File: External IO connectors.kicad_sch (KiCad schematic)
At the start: 2 parts

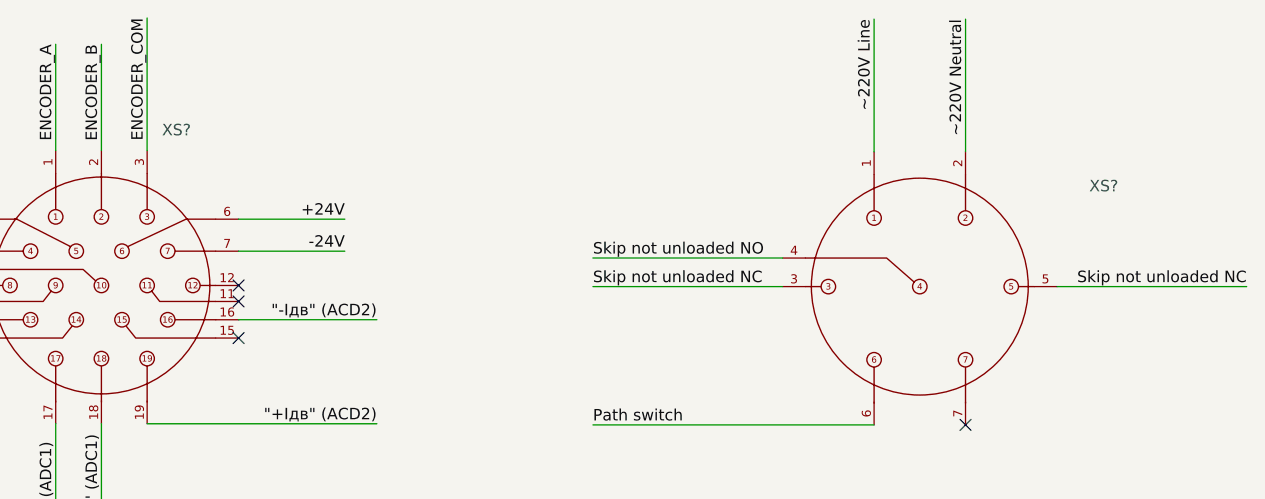
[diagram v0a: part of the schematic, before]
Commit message: Skip unload COM signal of external connector corrected
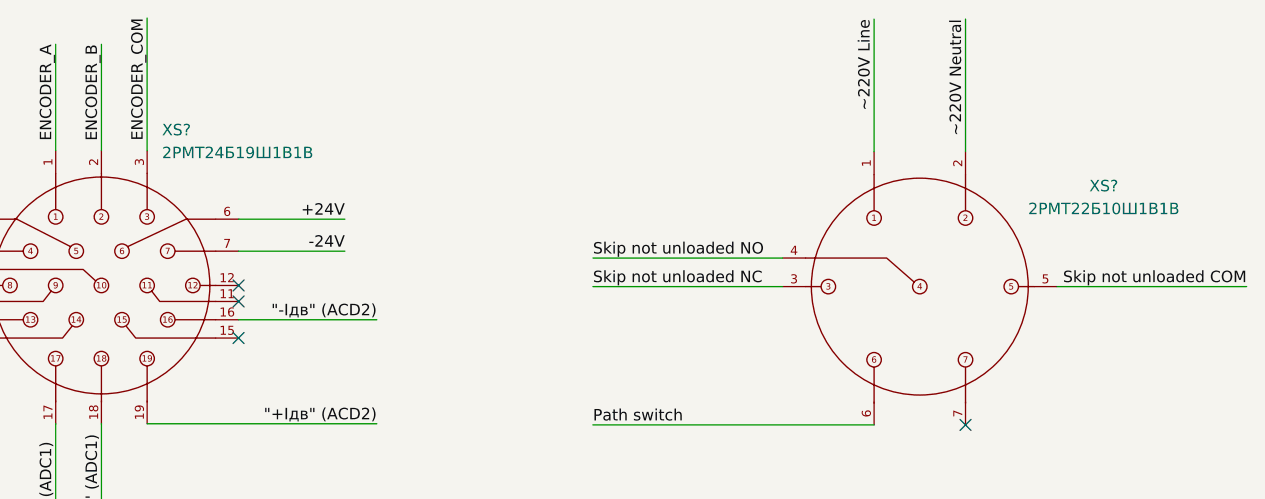
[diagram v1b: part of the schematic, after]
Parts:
- XS?: value (none) -> 2РМТ22Б10Ш1В1В
- XS?: value (none) -> 2РМТ24Б19Ш1В1В
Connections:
- net Skip not unloaded NC: no longer XS?.5
- new net Skip not unloaded COM: XS?.5
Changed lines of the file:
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@@
     (effects (font (size 1.27 1.27)) (justify right bottom))
   )
-  (label "Skip not unloaded NC" (at 222.377 96.139 180)
+  (label "Skip not unloaded COM" (at 222.377 96.139 180)
     (effects (font (size 1.27 1.27)) (justify right bottom))
   )
@@
     (in_bom yes) (on_board yes)
     (property "Reference" "XS?" (id 0) (at 206.502 84.963 0))
-    (property "Value" "" (id 1) (at 206.502 87.503 0))
+    (property "Value" "2РМТ22Б10Ш1В1В" (id 1) (at 206.502 87.503 0))
     (property "Footprint" "" (id 2) (at 186.055 96.139 0)
       (effects (font (size 1.27 1.27)) hide)
@@
       (effects (font (size 1.27 1.27)) (justify left))
     )
-    (property "Value" "" (id 1) (at 101.8541 81.28 0)
+    (property "Value" "2РМТ24Б19Ш1В1В" (id 1) (at 101.8541 81.28 0)
       (effects (font (size 1.27 1.27)) (justify left))
     )

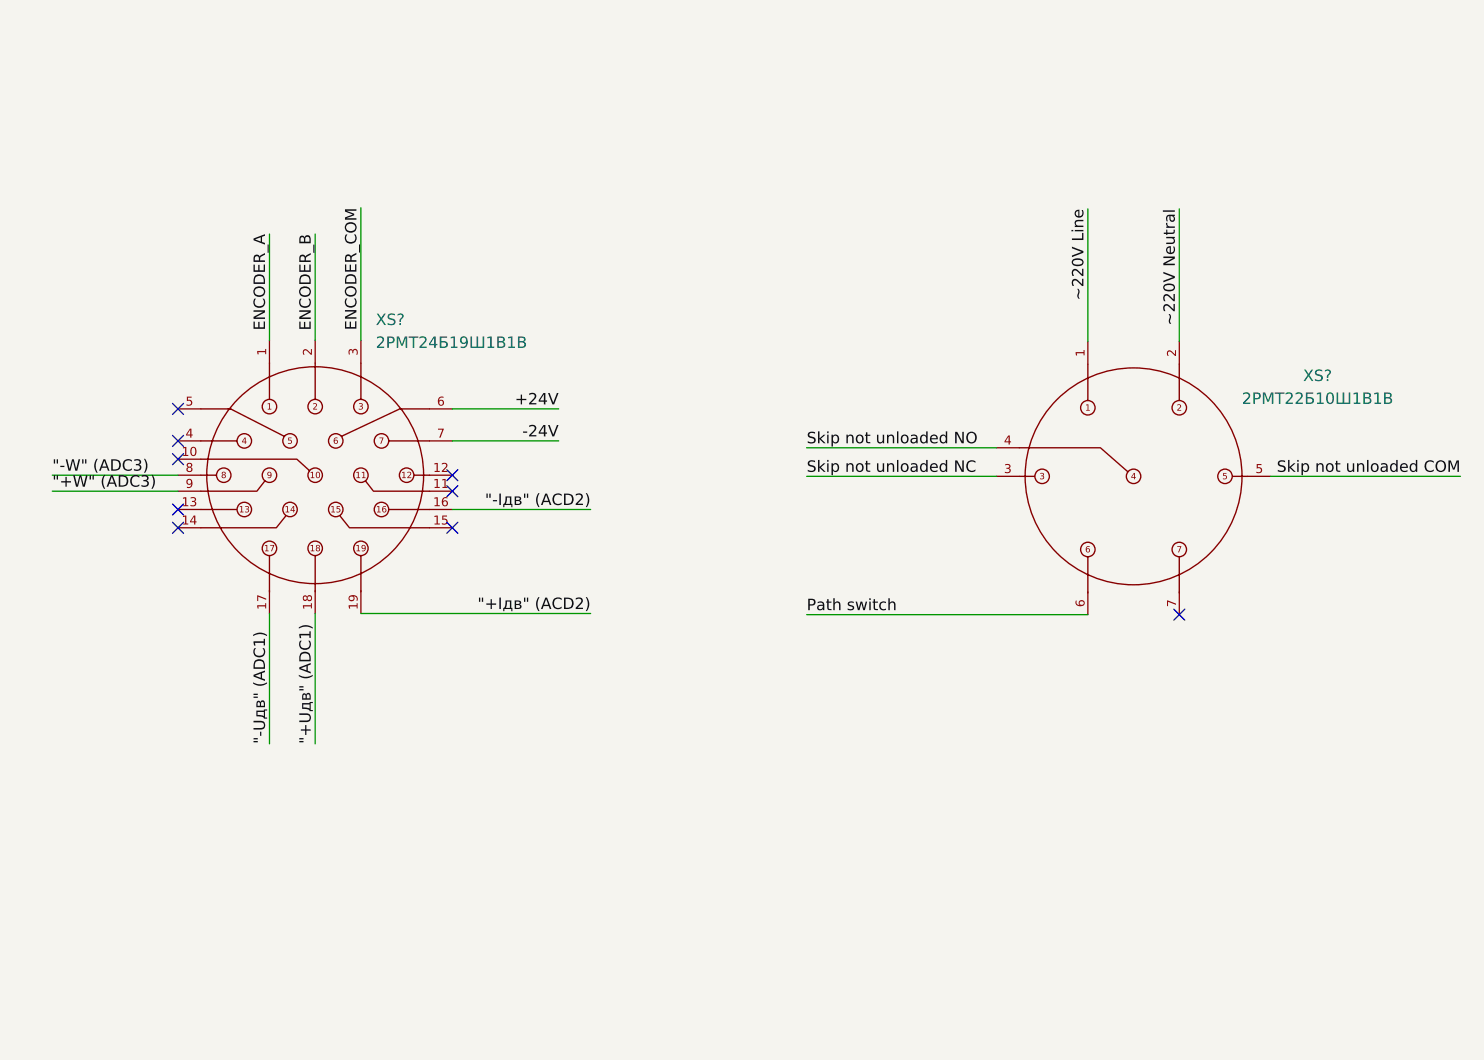
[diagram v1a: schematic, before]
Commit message: CPU programming external connector added
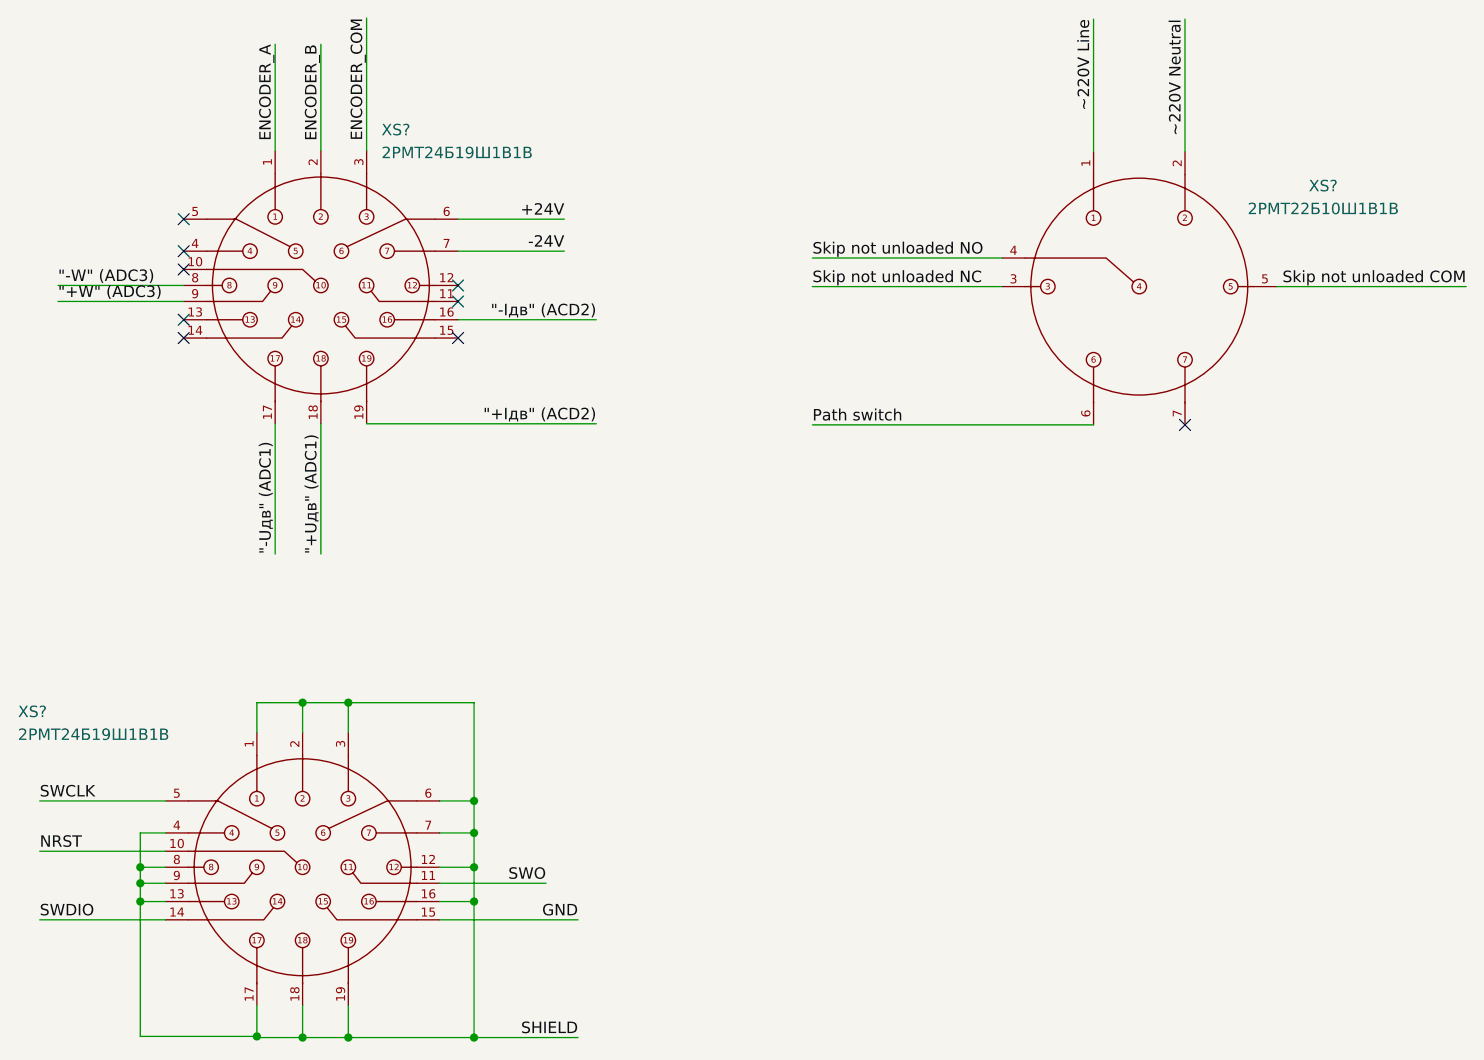
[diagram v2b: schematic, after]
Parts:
- added XS?: 2РМТ24Б19Ш1В1В, symbol SVIELCOM_Library:2РМТ24Б19Ш1В1В
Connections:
- new net GND: XS?.15
- new net NRST: XS?.10
- new net SHIELD: XS?.1, XS?.12, XS?.13, XS?.16, XS?.17, XS?.18, XS?.19, XS?.2, XS?.3, XS?.4, XS?.6, XS?.7, XS?.8, XS?.9
- new net SWCLK: XS?.5
- new net SWDIO: XS?.14
- new net SWO: XS?.11
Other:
- moved on the sheet: XS?
